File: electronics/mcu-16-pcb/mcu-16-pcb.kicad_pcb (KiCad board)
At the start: 2 copper layers, 6.4 x 0.7 mm, 32 parts, among them J1 HRO_TYPE-C-31-M-12, J2 FFC Connector, U1 AP2112K-3.3, U2 W25Q64JVXGIQ, U3 Raspberry_Pi_RP2040, Y1 12MHz

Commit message: WIP Update
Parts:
- moved U1 46.8 mm to (28.2, 29.6), turned to 180 degrees
- moved C15 38.3 mm to (28.7, 27.1), turned to 180 degrees
- moved C12 38.2 mm to (36.2, 34.1), turned to 90 degrees
- moved C11 37.4 mm to (35.2, 34.1), turned to 90 degrees
- moved C16 36.0 mm to (30.4, 30.7), turned to 90 degrees
- moved U2 36.0 mm to (29.4, 35.3)
- moved C14 32.8 mm to (34.2, 34.1), turned to 90 degrees
- moved C5 32.4 mm to (31.4, 39.1), turned to -90 degrees
- moved C6 32.2 mm to (31.4, 41.4), turned to 90 degrees
- moved C3 30.5 mm to (40.7, 36.2)
- moved C4 30.3 mm to (39.2, 35.3), turned to 90 degrees
- moved C10 29.7 mm to (41.0, 37.2)
- moved Y1 29.6 mm to (32.9, 46.9)
- moved SW_B1 29.5 mm to (28.0, 41.0)
- moved SW_R1 28.6 mm to (28.0, 51.0), turned to 180 degrees
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- renumbered C3 to C1, C14 to C10, C15 to C11, C16 to C12, C5 to C13, C6 to C14, C1 to C15, C2 to C16, C4 to C2, C8 to C3, C7 to C4, C9 to C5, C10 to C6, C11 to C7, C12 to C8, C13 to C9, R7 to R1, R8 to R2, R2 to R3, R1 to R4, R3 to R5, R5 to R6, R4 to R7, R6 to R8
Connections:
- R4 pad 2: Net-(R1-Pad2) -> Net-(R4-Pad2)
- SW_B1 pad 1: Net-(R1-Pad2) -> ~{USB_BOOT}
- SW_B1 pad 2: ~{USB_BOOT} -> Net-(R4-Pad2)
- U3 pad 13: unconnected-(U3-GPIO10-Pad13) -> COL7
- U3 pad 14: unconnected-(U3-GPIO11-Pad14) -> COL6
- U3 pad 17: COL7 -> unconnected-(U3-GPIO14-Pad17)
- U3 pad 18: COL6 -> unconnected-(U3-GPIO15-Pad18)
- U3 pad 2: COL7 -> unconnected-(U3-GPIO0-Pad2)
- U3 pad 3: COL8 -> unconnected-(U3-GPIO1-Pad3)
- U3 pad 4: COL9 -> unconnected-(U3-GPIO2-Pad4)
- U3 pad 5: ROW2 -> unconnected-(U3-GPIO3-Pad5)
- U3 pad 6: COL10 -> unconnected-(U3-GPIO4-Pad6)
- U3 pad 7: COL11 -> unconnected-(U3-GPIO5-Pad7)
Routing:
- net GND: track 0.00 -> 0.78 mm, vias 0 -> 14
- net Net-(U3-RUN): vias 0 -> 1
- net +3V3: vias 0 -> 5
- net +1V1: vias 0 -> 2
- added copper zone on B.Cu, net GND
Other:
- board size 6.4 x 0.7 mm -> 24 x 36 mm
- board text added: "B"

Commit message: Update MCU 16 pcb
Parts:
- added REF**: MountingHole_2.2mm_M2, MountingHole:MountingHole_2.2mm_M2, F.Cu at (27.0, 57.0)
- added REF**: MountingHole_2.2mm_M2, MountingHole:MountingHole_2.2mm_M2, F.Cu at (45.0, 33.0)
- added REF**: MountingHole_2.2mm_M2, MountingHole:MountingHole_2.2mm_M2, F.Cu at (45.0, 57.0)
- moved SW_R1 8.26 mm to (27.0, 42.8)
- moved SW_B1 2.06 mm to (27.0, 39.2)
- moved R3 1.54 mm to (25.5, 31.7), turned to 180 degrees
- moved R4 1.00 mm to (30.4, 39.1), turned to -90 degrees
- moved U2 0.99 mm to (28.7, 34.6)
- moved C3 0.98 mm to (40.2, 35.3), turned to 90 degrees
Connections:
- SW_B1 pad 3: GND -> unconnected-(SW_B1-Pad3)
- SW_B1 pad 4: unconnected-(SW_B1-Pad4) -> GND
- U3 pad 39: ROW2 -> ROW0
- U3 pad 41: ROW0 -> ROW2
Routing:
- net GND: track 0.78 -> 0.00 mm, vias 14 -> 20
- net Net-(U3-RUN): vias 1 -> 2
- added copper zone on F.Cu, net GND
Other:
- board text added: "1.0.0+20240715"
- board text added: "@takayoshiotake"
- board text added: "JLCJLCJLCJLC"
- board text added: "MCU 16"
- board text added: "R"

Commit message: Update MCU 16 pcb
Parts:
- added REF**: MountingHole_2.2mm_M2, MountingHole:MountingHole_2.2mm_M2, F.Cu at (45.0, 37.0)
- added REF**: MountingHole_2.2mm_M2, MountingHole:MountingHole_2.2mm_M2, F.Cu at (45.0, 32.0)
- moved REF** 6.00 mm to (45.0, 27.0)
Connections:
- net ROW4 renamed COL10
- net ROW5 renamed COL11
- J2 pad 1: COL7 -> ROW0
- J2 pad 10: ROW6 -> ROW3
- J2 pad 13: ROW3 -> COL9
- J2 pad 14: ROW2 -> COL8
- J2 pad 15: ROW1 -> COL7
- J2 pad 16: ROW0 -> COL6
- J2 pad 2: COL6 -> ROW1
- J2 pad 3: COL5 -> ROW2
- J2 pad 4: COL4 -> COL5
- J2 pad 5: COL3 -> COL4
- J2 pad 6: COL2 -> COL3
- J2 pad 7: COL1 -> COL2
- J2 pad 8: COL0 -> COL1
- J2 pad 9: ROW7 -> COL0
- U3 pad 13: COL7 -> ROW0
- U3 pad 14: COL6 -> ROW1
- U3 pad 27: COL5 -> ROW2
- U3 pad 28: COL4 -> COL5
- U3 pad 29: COL3 -> COL4
- U3 pad 30: COL2 -> COL3
- U3 pad 31: COL1 -> COL2
- U3 pad 32: COL0 -> COL1
- U3 pad 34: ROW7 -> COL0
- U3 pad 35: ROW6 -> ROW3
- U3 pad 38: ROW3 -> COL9
- U3 pad 39: ROW0 -> COL6
- U3 pad 40: ROW1 -> COL7
- U3 pad 41: ROW2 -> COL8
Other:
- board text added: "1.0.0+20240716"
- board text removed: "1.0.0+20240715"

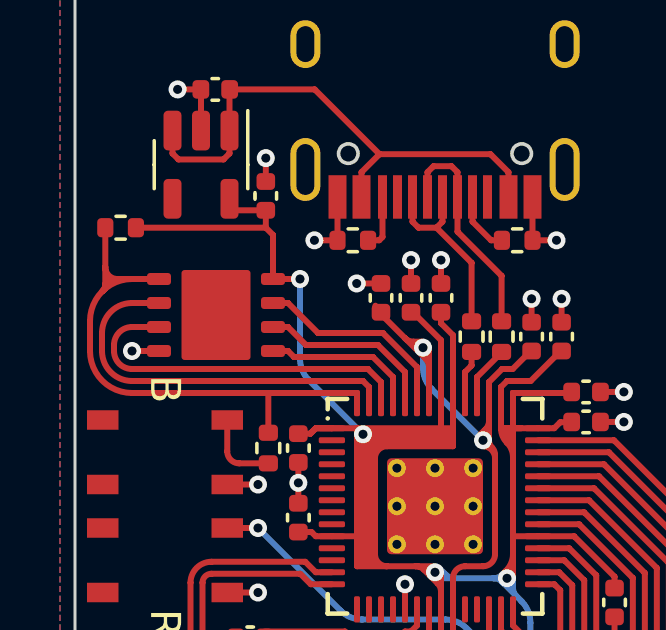
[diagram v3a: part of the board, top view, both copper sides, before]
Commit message: Add MCU 16 files
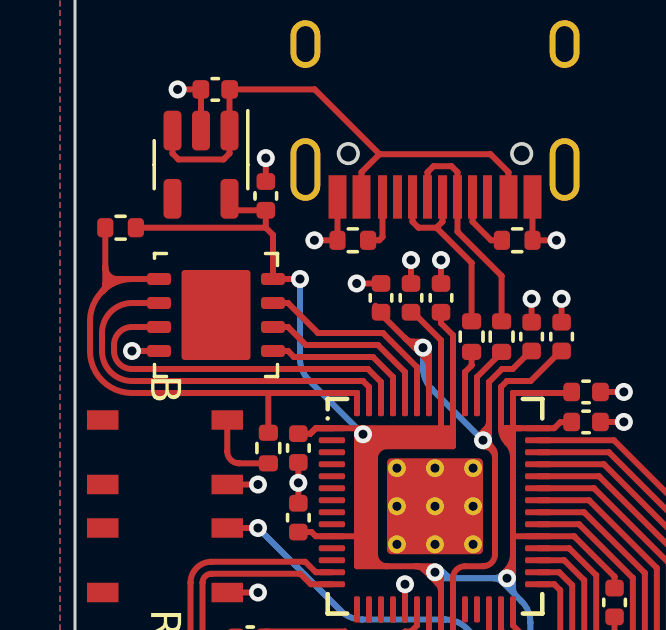
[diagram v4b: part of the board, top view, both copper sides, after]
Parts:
- turned U1 to 0 degrees
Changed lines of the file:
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@@
 			)
 		)
-		(property "LCSC" "C470426"
+		(property "LCSC" "C115360"
 			(at 0 0 0)
 			(unlocked yes)
@@
 		(attr smd)
 		(fp_line
+			(start -2.05 -2.05)
+			(end -2.05 -1.89)
+			(stroke
+				(width 0.12)
+				(type default)
+			)
+			(layer "F.SilkS")
+		)
+		(fp_line
+			(start -2.05 -2.05)
+			(end -1.65 -2.05)
+			(stroke
+				(width 0.12)
+				(type default)
+			)
+			(layer "F.SilkS")
+		)
+		(fp_line
+			(start -2.05 -1.65)
+			(end -2.05 -1.65)
+			(stroke
+				(width 0.12)
+				(type default)
+			)
+			(layer "F.SilkS")
+		)
+		(fp_line
+			(start -2.05 2.05)
+			(end -2.05 1.65)
+			(stroke
+				(width 0.12)
+				(type default)
+			)
+			(layer "F.SilkS")
+		)
+		(fp_line
+			(start -2.05 2.05)
+			(end -1.65 2.05)
+			(stroke
+				(width 0.12)
+				(type default)
+			)
+			(layer "F.SilkS")
+		)
+		(fp_line
+			(start 2.05 -2.05)
+			(end 1.65 -2.05)
+			(stroke
+				(width 0.12)
+				(type default)
+			)
+			(layer "F.SilkS")
+		)
+		(fp_line
+			(start 2.05 -2.05)
+			(end 2.05 -1.65)
+			(stroke
+				(width 0.12)
+				(type default)
+			)
+			(layer "F.SilkS")
+		)
+		(fp_line
+			(start 2.05 1.65)
+			(end 2.05 2.05)
+			(stroke
+				(width 0.12)
+				(type default)
+			)
+			(layer "F.SilkS")
+		)
+		(fp_line
+			(start 2.05 2.05)
+			(end 1.65 2.05)
+			(stroke
+				(width 0.12)
+				(type default)
+			)
+			(layer "F.SilkS")
+		)
+		(fp_line
 			(start -2.5 -2.25)
 			(end -2.5 2.25)
@@
 			)
 		)
-		(property "LCSC" "C470426"
+		(property "LCSC" "C115360"
 			(at 0 0 180)
 			(unlocked yes)
@@
 	(footprint "Project_Library:SOT-23-5"
 		(layer "F.Cu")
-		(at 28.2 29.615 180)
+		(at 28.2 29.615)
 		(descr "SOT, 5 Pin (https://www.jedec.org/sites/default/files/docs/Mo-178c.PDF variant AA), generated with kicad-footprint-generator ipc_gullwing_generator.py")
 		(tags "SOT TO_SOT_SMD")
 		(property "Reference" "U1"
-			(at 0 -2.8 0)
+			(at 0 -2.8 360)
 			(layer "F.SilkS")
 			(hide yes)
@@
 		)
 		(property "Value" "AP2112K-3.3"
-			(at 0 2.8 0)
+			(at 0 2.8 360)
 			(layer "F.Fab")
 			(hide yes)
@@
 		)
 		(property "Footprint" "Project_Library:SOT-23-5"
-			(at 0 0 0)
+			(at 0 0 360)
 			(layer "F.Fab")
 			(hide yes)
@@
 		)
 		(property "Datasheet" "https://www.diodes.com/assets/Datasheets/AP2112.pdf"
-			(at 0 0 0)
+			(at 0 0 360)
 			(layer "F.Fab")
 			(hide yes)
@@
 		)
 		(property "Description" ""
-			(at 0 0 0)
+			(at 0 0 360)
 			(layer "F.Fab")
 			(hide yes)
@@
 		)
 		(property "LCSC" "C51118"
-			(at 0 0 180)
+			(at 0 0 0)
 			(unlocked yes)
 			(layer "F.Fab")
@@
 		(attr smd)
 		(fp_line
-			(start 1.56 0)
-			(end 1.56 0.8)
+			(start -1.56 0)
+			(end -1.56 -0.8)
 			(stroke
 				(width 0.12)
@@
 		)
 		(fp_line
-			(start 1.56 0)
-			(end 1.56 -0.8)
+			(start -1.56 0)
+			(end -1.56 0.8)
 			(stroke
 				(width 0.12)
@@
 		)
 		(fp_line
-			(start -1.56 0)
-			(end -1.56 1.8)
+			(start 1.56 0)
+			(end 1.56 -1.8)
 			(stroke
 				(width 0.12)
@@
 		)
 		(fp_line
-			(start -1.56 0)
-			(end -1.56 -0.8)
+			(start 1.56 0)
+			(end 1.56 0.8)
 			(stroke
 				(width 0.12)
@@
 		)
 		(fp_line
-			(start 1.7 2.05)
-			(end 1.7 -2.05)
+			(start -1.7 -2.05)
+			(end -1.7 2.05)
 			(stroke
 				(width 0.05)
@@
 		)
 		(fp_line
-			(start 1.7 -2.05)
-			(end -1.7 -2.05)
+			(start -1.7 2.05)
+			(end 1.7 2.05)
 			(stroke
 				(width 0.05)
@@
 		)
 		(fp_line
-			(start -1.7 2.05)
-			(end 1.7 2.05)
+			(start 1.7 -2.05)
+			(end -1.7 -2.05)
 			(stroke
 				(width 0.05)
@@
 		)
 		(fp_line
-			(start -1.7 -2.05)
-			(end -1.7 2.05)
+			(start 1.7 2.05)
+			(end 1.7 -2.05)
 			(stroke
 				(width 0.05)
@@
 		)
 		(fp_line
-			(start 1.45 0.8)
-			(end -1.05 0.8)
+			(start -1.45 -0.8)
+			(end 1.05 -0.8)
 			(stroke
 				(width 0.1)
@@
 		)
 		(fp_line
-			(start 1.45 -0.8)
-			(end 1.45 0.8)
+			(start -1.45 0.8)
+			(end -1.45 -0.8)
 			(stroke
 				(width 0.1)
@@
 		)
 		(fp_line
-			(start -1.05 0.8)
-			(end -1.45 0.4)
+			(start 1.05 -0.8)
+			(end 1.45 -0.4)
 			(stroke
 				(width 0.1)
@@
 		)
 		(fp_line
-			(start -1.45 0.4)
-			(end -1.45 -0.8)
+			(start 1.45 -0.4)
+			(end 1.45 0.8)
 			(stroke
 				(width 0.1)
@@
 		)
 		(fp_line
-			(start -1.45 -0.8)
-			(end 1.45 -0.8)
+			(start 1.45 0.8)
+			(end -1.45 0.8)
 			(stroke
 				(width 0.1)
@@
 		)
 		(fp_text user "${REFERENCE}"
-			(at 0 0 0)
+			(at 0 0 360)
 			(layer "F.Fab")
 			(effects
@@
 		)
 		(pad "1" smd roundrect
-			(at -0.95 1.1375 270)
+			(at 0.95 -1.1375 270)
 			(size 1.325 0.6)
 			(layers "F.Cu" "F.Paste" "F.Mask")
@@
 		)
 		(pad "2" smd roundrect
-			(at 0 1.1375 270)
+			(at 0 -1.1375 270)
 			(size 1.325 0.6)
 			(layers "F.Cu" "F.Paste" "F.Mask")
@@
 		)
 		(pad "3" smd roundrect
-			(at 0.95 1.1375 270)
+			(at -0.95 -1.1375 270)
 			(size 1.325 0.6)
 			(layers "F.Cu" "F.Paste" "F.Mask")
@@
 		)
 		(pad "4" smd roundrect
-			(at 0.95 -1.1375 270)
+			(at -0.95 1.1375 270)
 			(size 1.325 0.6)
 			(layers "F.Cu" "F.Paste" "F.Mask")
@@
 		)
 		(pad "5" smd roundrect
-			(at -0.95 -1.1375 270)
+			(at 0.95 1.1375 270)
 			(size 1.325 0.6)
 			(layers "F.Cu" "F.Paste" "F.Mask")
